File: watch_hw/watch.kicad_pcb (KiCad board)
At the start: 6 copper layers, 36.4 x 38.8 mm, 55 parts, among them J1 USB_B_Micro, J3 Conn_ARM_SWD_TagConnect_TC203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, SW1 TL6340AF160Q, SW2 TL6340AF160Q, U1 STM32WB55CGUx, U2 nPM1100-QDAA, U3 MAX17048G+, U4 BMA456, U5 MAXM86161EFD+T, X1 NX2016SA-32M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

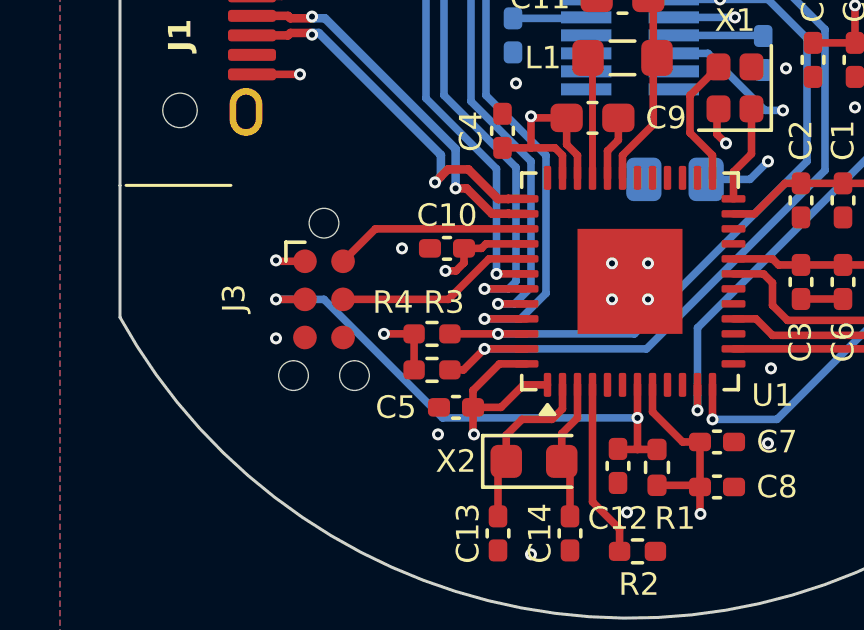
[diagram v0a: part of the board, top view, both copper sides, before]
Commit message: move tagconnect slightly
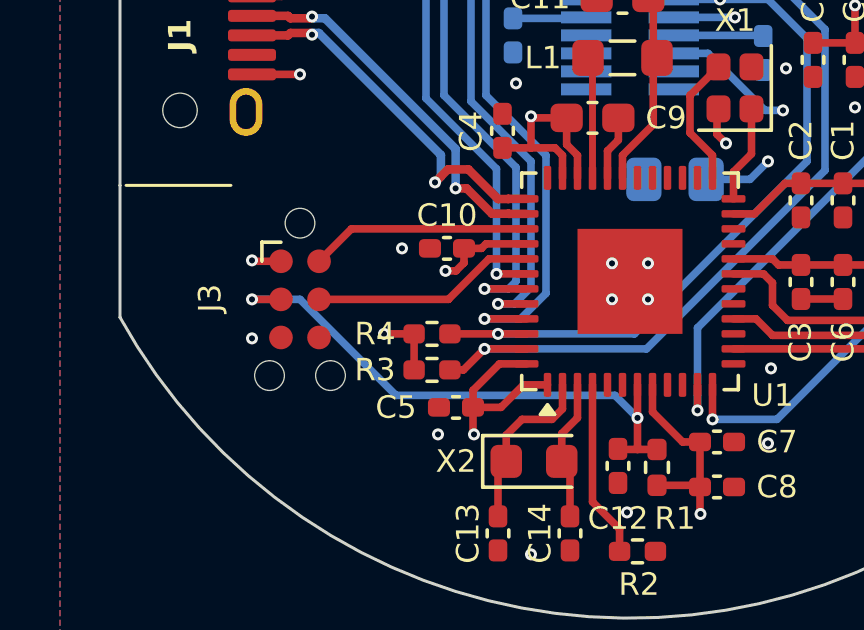
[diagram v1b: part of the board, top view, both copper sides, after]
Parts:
- moved J3 0.80 mm to (139.0, 108.8)
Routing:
- net /SoC/SWCLK: track 6.67 -> 7.47 mm
- net /SoC/SWDIO: track 6.56 -> 7.36 mm
- net /SoC/NRST: track 18.1 -> 18.9 mm
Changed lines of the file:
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@@
 	(footprint "Connector:Tag-Connect_TC2030-IDC-NL_2x03_P1.27mm_Vertical"
 		(layer "F.Cu")
-		(at 139.8 108.8 -90)
+		(at 139 108.8 -90)
 		(descr "Tag-Connect programming header; http://www.tag-connect.com/Materials/TC2030-IDC-NL.pdf")
 		(tags "tag connect programming header pogo pins")
@@
 			(polygon
 				(pts
-					(xy 140.435 110.07) (xy 140.435 107.53) (xy 139.165 107.53) (xy 139.165 110.07)
+					(xy 139.635 110.07) (xy 139.635 107.53) (xy 138.365 107.53) (xy 138.365 110.07)
 				)
 			)
@@
 		(model "${KIPRJMOD}/lib/3d/LS012B7DH02.step"
 			(offset
-				(xyz 0 0 1.5)
+				(xyz 0 0 4.5)
 			)
 			(scale
@@
 			)
 			(rotate
-				(xyz 0 0 0)
+				(xyz -0 -0 -0)
 			)
 		)
@@
 		(tags "resistor handsolder")
 		(property "Reference" "R4"
-			(at -1.3 -1.05 0)
+			(at -1.9 0 0)
 			(layer "F.SilkS")
 			(effects
@@
 		(tags "resistor handsolder")
 		(property "Reference" "R3"
-			(at 0.4 -2.25 0)
+			(at -1.9 0 0)
 			(layer "F.SilkS")
 			(effects
@@
 	)
 	(via
-		(at 138.2 110.1)
+		(at 137.4 110.1)
 		(size 0.4)
 		(drill 0.2)
@@
 	)
 	(segment
-		(start 139.165 107.53)
-		(end 138.23 107.53)
+		(start 138.365 107.53)
+		(end 137.43 107.53)
 		(width 0.254)
 		(layer "F.Cu")
@@
 	)
 	(segment
-		(start 138.23 107.53)
-		(end 138.2 107.5)
+		(start 137.43 107.53)
+		(end 137.4 107.5)
 		(width 0.254)
 		(layer "F.Cu")
@@
 	)
 	(via
-		(at 138.2 107.5)
+		(at 137.4 107.5)
 		(size 0.4)
 		(drill 0.2)
@@
 	)
 	(segment
-		(start 139.165 108.8)
-		(end 138.2 108.8)
+		(start 138.365 108.8)
+		(end 137.4 108.8)
 		(width 0.254)
 		(layer "F.Cu")
@@
 	)
 	(via
-		(at 138.2 108.8)
+		(at 137.4 108.8)
 		(size 0.4)
 		(drill 0.2)
@@
 	)
 	(segment
-		(start 143.75 112.75)
-		(end 139.8 108.8)
+		(start 142.2 112)
+		(end 149.5 112)
 		(width 0.254)
 		(layer "B.Cu")
@@
 	)
 	(segment
-		(start 139.8 108.8)
-		(end 138.2 108.8)
+		(start 149.5 112)
+		(end 150.25 112.75)
 		(width 0.254)
 		(layer "B.Cu")
@@
 	)
 	(segment
-		(start 150.25 112.75)
-		(end 143.75 112.75)
+		(start 139 108.8)
+		(end 142.2 112)
+		(width 0.254)
+		(layer "B.Cu")
+		(net 53)
+	)
+	(segment
+		(start 139 108.8)
+		(end 137.4 108.8)
 		(width 0.254)
 		(layer "B.Cu")
@@
 	)
 	(segment
-		(start 141.515 106.45)
-		(end 140.435 107.53)
+		(start 140.715 106.45)
+		(end 146.55 106.45)
 		(width 0.254)
 		(layer "F.Cu")
@@
 	)
 	(segment
-		(start 146.55 106.45)
-		(end 141.515 106.45)
+		(start 140.715 106.45)
+		(end 139.635 107.53)
 		(width 0.254)
 		(layer "F.Cu")
@@
 	)
 	(segment
-		(start 143.95 108.8)
-		(end 145.3 107.45)
+		(start 145.3 107.45)
+		(end 146.55 107.45)
 		(width 0.254)
 		(layer "F.Cu")
@@
 	)
 	(segment
-		(start 140.435 108.8)
-		(end 143.95 108.8)
+		(start 143.95 108.8)
+		(end 139.635 108.8)
 		(width 0.254)
 		(layer "F.Cu")
@@
 	)
 	(segment
-		(start 145.3 107.45)
-		(end 146.55 107.45)
+		(start 143.95 108.8)
+		(end 145.3 107.45)
 		(width 0.254)
 		(layer "F.Cu")

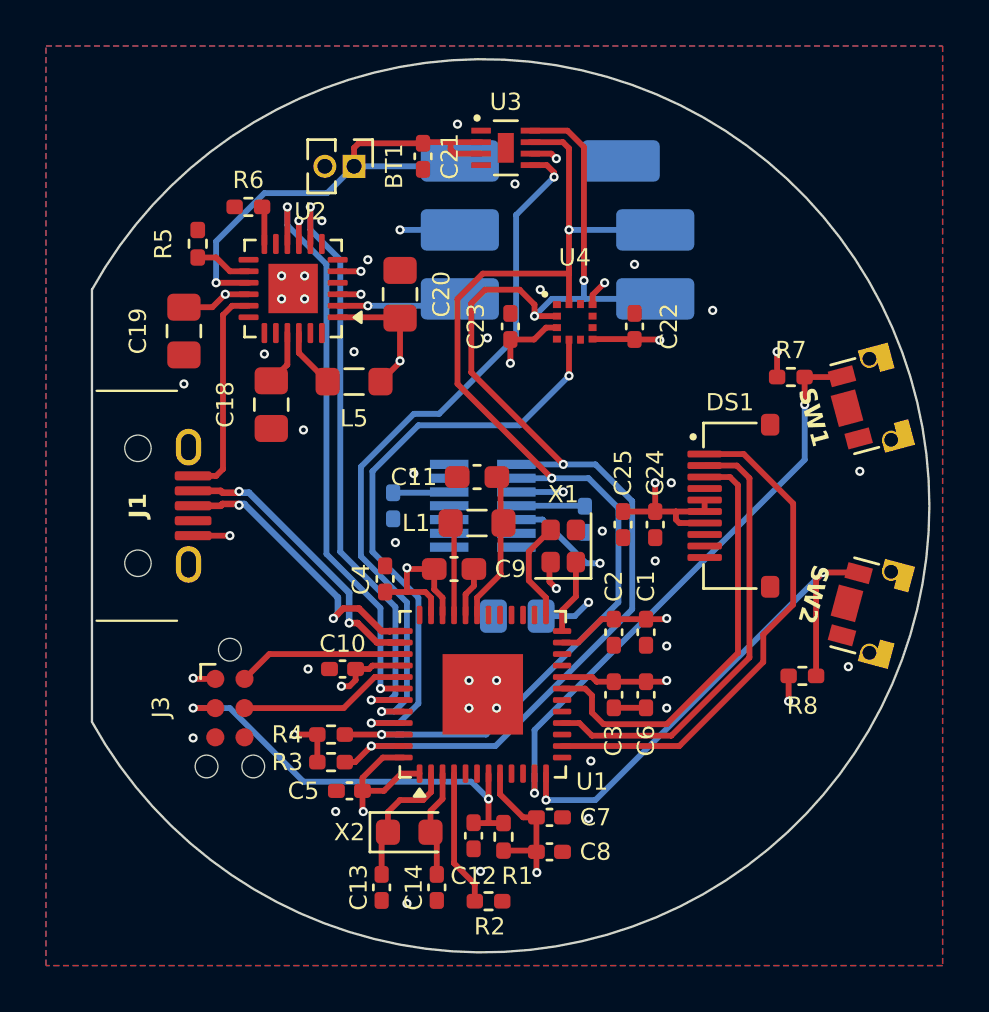
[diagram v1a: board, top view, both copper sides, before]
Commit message: Slightly increase silkscreen text size
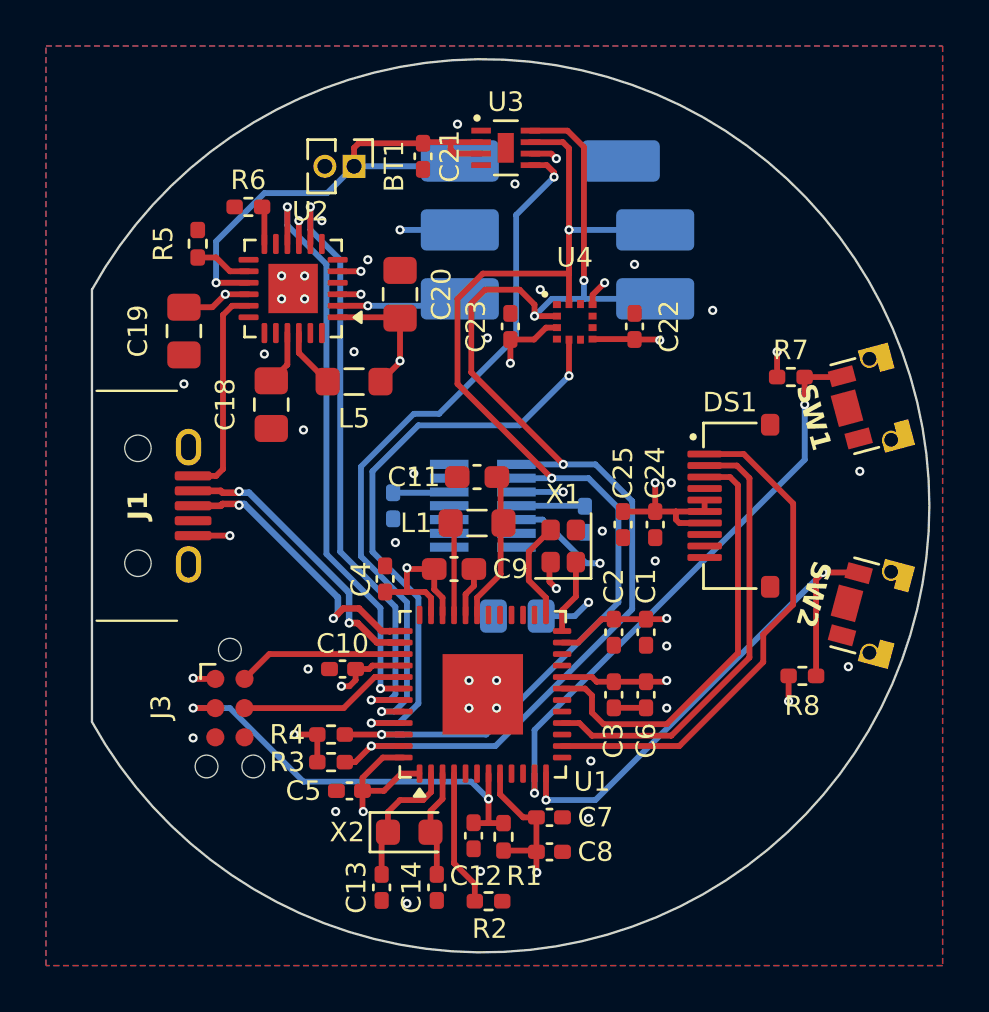
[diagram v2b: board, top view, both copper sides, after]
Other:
- board text added: "Brian Cruz"
- board text added: "V01"

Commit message: Add ouroboros art
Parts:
- added G***: LOGO, watch:ouroboros, B.Cu at (158.9, 109.1)

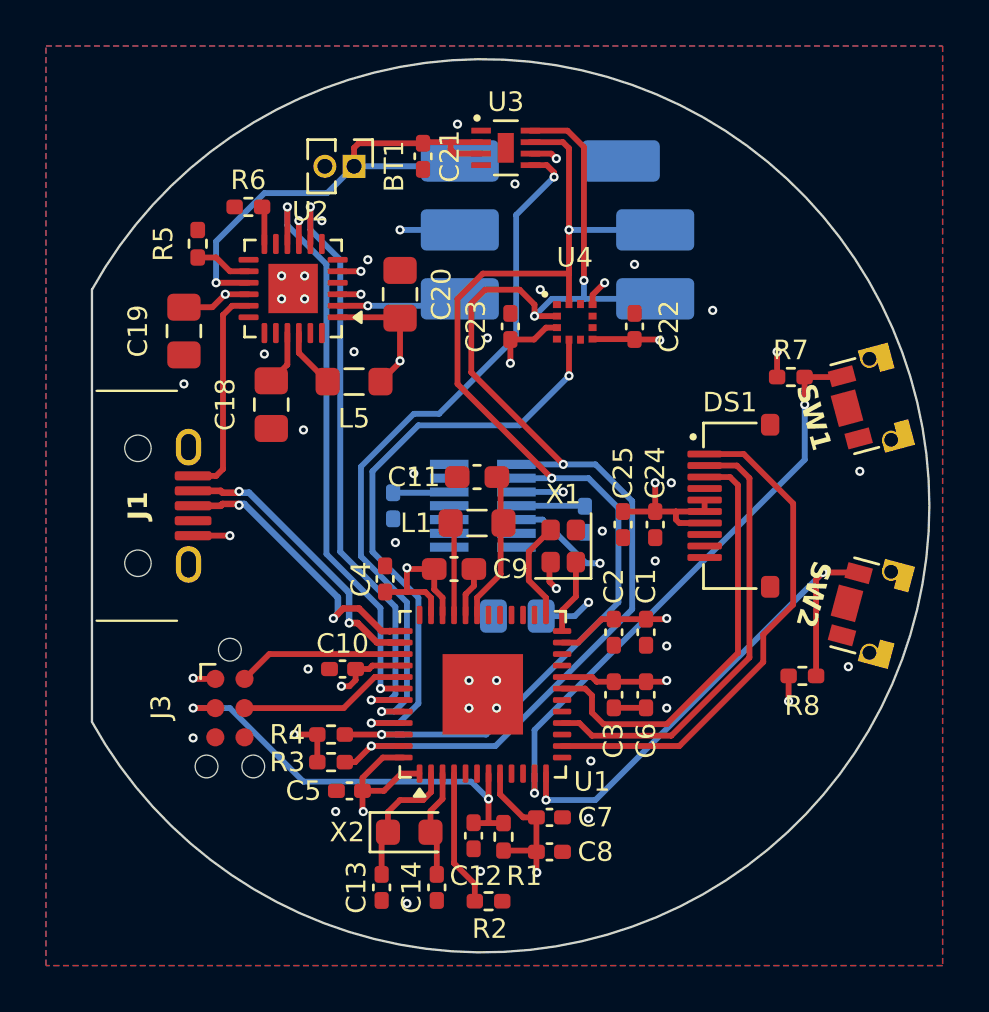
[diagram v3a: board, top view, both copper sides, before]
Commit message: Expand via size for JLC
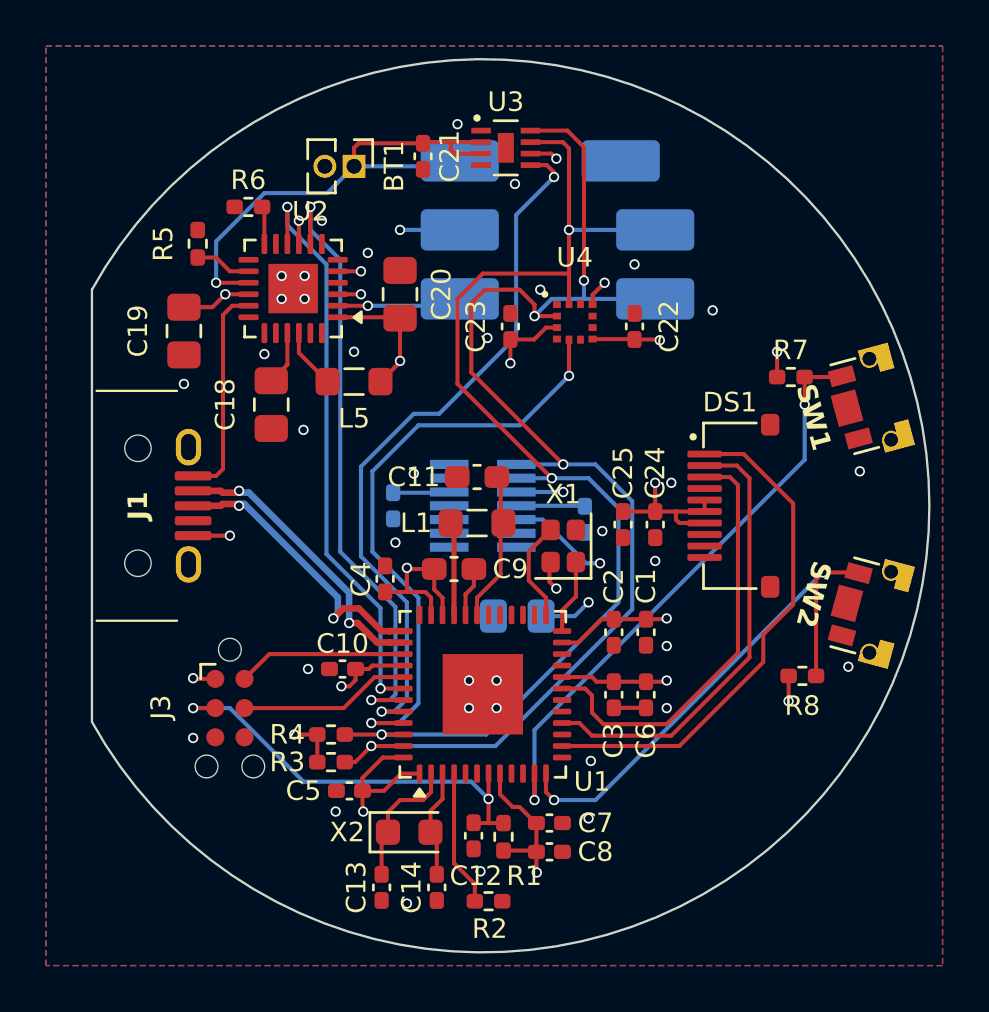
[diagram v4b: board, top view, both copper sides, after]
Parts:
- C21, C22, C23: value 0.1uF -> 100nF
- J1: value USB_B_Micro -> UJ2-MIBH-4-SMT-TR-67
- R6: value 560R -> 680R
- moved C7 0.25 mm to (152.9, 113.8)
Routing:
- net /BTN0: track 25.7 -> 26.3 mm
